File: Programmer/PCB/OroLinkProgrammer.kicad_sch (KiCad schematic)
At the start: 17 parts, among them IC1 SE555DR, J1 67996-110HLF, M1 STM32 STLINK V3MODS

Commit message: re-layout board onto new PCB
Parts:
- removed H1, H2, H3: MountingHole, MountingHole:MountingHole_3.2mm_M3_Pad_Via, symbol Mechanical:MountingHole
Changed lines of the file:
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@@
   )
   (text "NOTE: BOM COMPONENTS DO NOT INCLUDE\n        2x5 2.54mm-PITCH CABLE TERMINAL,\n        BUT ONE IS REQUIRED (CHECK\n        PCB FOR PINOUT, AND TAKE\n        NOTE OF NOTCH SPECIFICATION)"
-    (at 191.77 147.32 0)
+    (at 177.165 147.955 0)
     (effects (font (size 1.27 1.27)) (justify left bottom))
   )
@@
         (path "/fd4a9034-ad51-4795-b47c-26ad06998c0c"
           (reference "#PWR02") (unit 1)
-        )
-      )
-    )
-  )
-  (symbol (lib_id "Mechanical:MountingHole") (at 165.735 135.255 0) (unit 1)
-    (in_bom no) (on_board yes) (dnp no)
-    (property "Reference" "H2" (at 168.91 135.255 0)
-      (effects (font (size 1.27 1.27)) (justify left))
-    )
-    (property "Value" "MountingHole" (at 168.275 136.5323 0)
-      (effects (font (size 1.27 1.27)) (justify left) hide)
-    )
-    (property "Footprint" "MountingHole:MountingHole_3.2mm_M3_Pad_Via" (at 165.735 135.255 0)
-      (effects (font (size 1.27 1.27)) hide)
-    )
-    (property "Datasheet" "~" (at 165.735 135.255 0)
-      (effects (font (size 1.27 1.27)) hide)
-    )
-    (property "Sim.Enable" "0" (at 165.735 135.255 0)
-      (effects (font (size 1.27 1.27)) hide)
-    )
-    (instances
-      (project "OroLinkProgrammer"
-        (path "/fd4a9034-ad51-4795-b47c-26ad06998c0c"
-          (reference "H2") (unit 1)
-        )
-      )
-    )
-  )
-  (symbol (lib_id "Mechanical:MountingHole") (at 165.735 130.175 0) (unit 1)
-    (in_bom no) (on_board yes) (dnp no)
-    (property "Reference" "H1" (at 168.91 130.175 0)
-      (effects (font (size 1.27 1.27)) (justify left))
-    )
-    (property "Value" "MountingHole" (at 168.275 131.4523 0)
-      (effects (font (size 1.27 1.27)) (justify left) hide)
-    )
-    (property "Footprint" "MountingHole:MountingHole_3.2mm_M3_Pad_Via" (at 165.735 130.175 0)
-      (effects (font (size 1.27 1.27)) hide)
-    )
-    (property "Datasheet" "~" (at 165.735 130.175 0)
-      (effects (font (size 1.27 1.27)) hide)
-    )
-    (property "Sim.Enable" "0" (at 165.735 130.175 0)
-      (effects (font (size 1.27 1.27)) hide)
-    )
-    (instances
-      (project "OroLinkProgrammer"
-        (path "/fd4a9034-ad51-4795-b47c-26ad06998c0c"
-          (reference "H1") (unit 1)
         )
       )
@@
     )
   )
-  (symbol (lib_id "Mechanical:MountingHole") (at 165.735 140.335 0) (unit 1)
-    (in_bom no) (on_board yes) (dnp no)
-    (property "Reference" "H3" (at 168.91 140.335 0)
-      (effects (font (size 1.27 1.27)) (justify left))
-    )
-    (property "Value" "MountingHole" (at 168.275 141.6123 0)
-      (effects (font (size 1.27 1.27)) (justify left) hide)
-    )
-    (property "Footprint" "MountingHole:MountingHole_3.2mm_M3_Pad_Via" (at 165.735 140.335 0)
-      (effects (font (size 1.27 1.27)) hide)
-    )
-    (property "Datasheet" "~" (at 165.735 140.335 0)
-      (effects (font (size 1.27 1.27)) hide)
-    )
-    (property "Sim.Enable" "0" (at 165.735 140.335 0)
-      (effects (font (size 1.27 1.27)) hide)
-    )
-    (instances
-      (project "OroLinkProgrammer"
-        (path "/fd4a9034-ad51-4795-b47c-26ad06998c0c"
-          (reference "H3") (unit 1)
-        )
-      )
-    )
-  )
   (symbol (lib_id "SamacSys_Parts:SG73P2ATTD102J") (at 83.82 42.545 180) (unit 1)
     (in_bom yes) (on_board yes) (dnp no) (fields_autoplaced)
@@
     )
   )
-  (symbol (lib_id "Oro:BOM Part") (at 193.675 132.715 0) (unit 1)
+  (symbol (lib_id "Oro:BOM Part") (at 179.07 133.35 0) (unit 1)
     (in_bom yes) (on_board no) (dnp no)
-    (property "Reference" "B2" (at 195.58 132.0713 0)
-      (effects (font (size 1.27 1.27)) (justify left) hide)
-    )
-    (property "Value" "S-3-J-7-G" (at 196.215 133.985 0)
+    (property "Reference" "B2" (at 180.975 132.7063 0)
+      (effects (font (size 1.27 1.27)) (justify left) hide)
+    )
+    (property "Value" "S-3-J-7-G" (at 181.61 134.62 0)
       (effects (font (size 1.27 1.27)) (justify left))
     )
-    (property "Footprint" "" (at 193.675 132.715 0)
-      (effects (font (size 1.27 1.27)) hide)
-    )
-    (property "Datasheet" "https://www.mouser.de/datasheet/2/193/F_SINT_Board_Test_StandardSpringProbes_0125Centers-2308876.pdf" (at 193.675 132.715 0)
-      (effects (font (size 1.27 1.27)) hide)
-    )
-    (property "Sim.Enable" "0" (at 193.675 132.715 0)
-      (effects (font (size 1.27 1.27)) hide)
-    )
-    (property "Manufacturer_Part_Number" "R-3-CR" (at 193.675 132.715 0)
-      (effects (font (size 1.27 1.27)) hide)
-    )
-    (property "Mouser Part Number" "S-3-J-7-G" (at 193.675 132.715 0)
-      (effects (font (size 1.27 1.27)) hide)
-    )
-    (property "Note" "TEST PROBE" (at 196.215 132.715 0)
+    (property "Footprint" "" (at 179.07 133.35 0)
+      (effects (font (size 1.27 1.27)) hide)
+    )
+    (property "Datasheet" "https://www.mouser.de/datasheet/2/193/F_SINT_Board_Test_StandardSpringProbes_0125Centers-2308876.pdf" (at 179.07 133.35 0)
+      (effects (font (size 1.27 1.27)) hide)
+    )
+    (property "Sim.Enable" "0" (at 179.07 133.35 0)
+      (effects (font (size 1.27 1.27)) hide)
+    )
+    (property "Manufacturer_Part_Number" "R-3-CR" (at 179.07 133.35 0)
+      (effects (font (size 1.27 1.27)) hide)
+    )
+    (property "Mouser Part Number" "S-3-J-7-G" (at 179.07 133.35 0)
+      (effects (font (size 1.27 1.27)) hide)
+    )
+    (property "Note" "TEST PROBE" (at 181.61 133.35 0)
       (effects (font (size 1.27 1.27)) (justify left bottom))
     )
-    (property "BOM Qty" "6" (at 193.675 132.715 0)
+    (property "BOM Qty" "6" (at 179.07 133.35 0)
       (effects (font (size 1.27 1.27)) hide)
     )
@@
     )
   )
-  (symbol (lib_id "Oro:BOM Part") (at 193.675 125.73 0) (unit 1)
+  (symbol (lib_id "Oro:BOM Part") (at 179.07 126.365 0) (unit 1)
     (in_bom yes) (on_board no) (dnp no)
-    (property "Reference" "B2" (at 195.58 125.0863 0)
-      (effects (font (size 1.27 1.27)) (justify left) hide)
-    )
-    (property "Value" "R-3-CR" (at 196.215 127 0)
+    (property "Reference" "B2" (at 180.975 125.7213 0)
+      (effects (font (size 1.27 1.27)) (justify left) hide)
+    )
+    (property "Value" "R-3-CR" (at 181.61 127.635 0)
       (effects (font (size 1.27 1.27)) (justify left))
     )
-    (property "Footprint" "" (at 193.675 125.73 0)
-      (effects (font (size 1.27 1.27)) hide)
-    )
-    (property "Datasheet" "https://www.mouser.de/datasheet/2/193/ICDIS00002_1-2550070.pdf" (at 193.675 125.73 0)
-      (effects (font (size 1.27 1.27)) hide)
-    )
-    (property "Sim.Enable" "0" (at 193.675 125.73 0)
-      (effects (font (size 1.27 1.27)) hide)
-    )
-    (property "Manufacturer_Part_Number" "R-3-CR" (at 193.675 125.73 0)
-      (effects (font (size 1.27 1.27)) hide)
-    )
-    (property "Mouser Part Number" "818-R-3-CR" (at 193.675 125.73 0)
-      (effects (font (size 1.27 1.27)) hide)
-    )
-    (property "Note" "TEST PROBE CRIMP SOCKET" (at 196.215 125.73 0)
+    (property "Footprint" "" (at 179.07 126.365 0)
+      (effects (font (size 1.27 1.27)) hide)
+    )
+    (property "Datasheet" "https://www.mouser.de/datasheet/2/193/ICDIS00002_1-2550070.pdf" (at 179.07 126.365 0)
+      (effects (font (size 1.27 1.27)) hide)
+    )
+    (property "Sim.Enable" "0" (at 179.07 126.365 0)
+      (effects (font (size 1.27 1.27)) hide)
+    )
+    (property "Manufacturer_Part_Number" "R-3-CR" (at 179.07 126.365 0)
+      (effects (font (size 1.27 1.27)) hide)
+    )
+    (property "Mouser Part Number" "818-R-3-CR" (at 179.07 126.365 0)
+      (effects (font (size 1.27 1.27)) hide)
+    )
+    (property "Note" "TEST PROBE CRIMP SOCKET" (at 181.61 126.365 0)
       (effects (font (size 1.27 1.27)) (justify left bottom))
     )
-    (property "BOM Qty" "6" (at 193.675 125.73 0)
-      (effects (font (size 1.27 1.27)) hide)
-    )
+    (property "BOM Qty" "6" (at 179.07 126.365 0)
+      (effects (font (size 1.27 1.27)) hide)
+    )

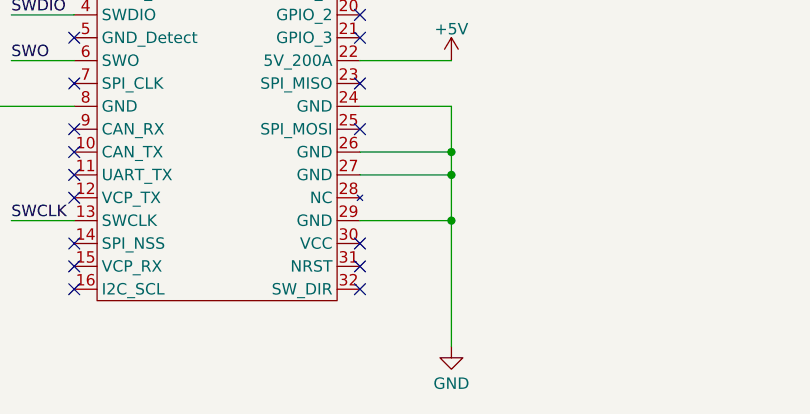
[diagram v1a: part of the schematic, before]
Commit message: tie NRST to ground on programmer (closes #4)
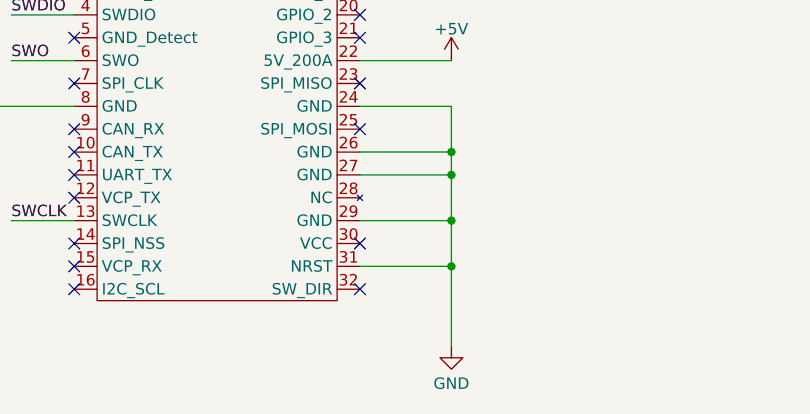
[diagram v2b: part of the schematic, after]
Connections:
- net GND: now also M1.31 (NRST)
- no-connect marks 33 -> 32
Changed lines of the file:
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@@
   (junction (at 229.235 93.345) (diameter 0) (color 0 0 0 0)
+  )
+  (junction (at 135.255 153.67) (diameter 0) (color 0 0 0 0)
   )
   (junction (at 186.69 55.88) (diameter 0) (color 0 0 0 0)
@@
   (no_connect (at 93.345 140.97))
   (no_connect (at 93.345 151.13))
-  (no_connect (at 125.095 153.67))
   (no_connect (at 93.345 156.21))
   (no_connect (at 125.095 118.11))
@@
   (no_connect (at 93.98 66.04))
   (no_connect (at 125.095 156.21))
+  (wire (pts (xy 125.095 153.67) (xy 135.255 153.67))
+    (stroke (width 0) (type default))
+  )
   (wire (pts (xy 43.815 42.545) (xy 47.625 42.545))
     (stroke (width 0) (type default))
@@
   )
   (wire (pts (xy 124.46 60.96) (xy 132.08 60.96))
+    (stroke (width 0) (type default))
+  )
+  (wire (pts (xy 135.255 153.67) (xy 135.255 162.56))
     (stroke (width 0) (type default))
   )
@@
     (stroke (width 0) (type default))
   )
-  (wire (pts (xy 135.255 148.59) (xy 135.255 162.56))
+  (wire (pts (xy 135.255 148.59) (xy 135.255 153.67))
     (stroke (width 0) (type default))
   )

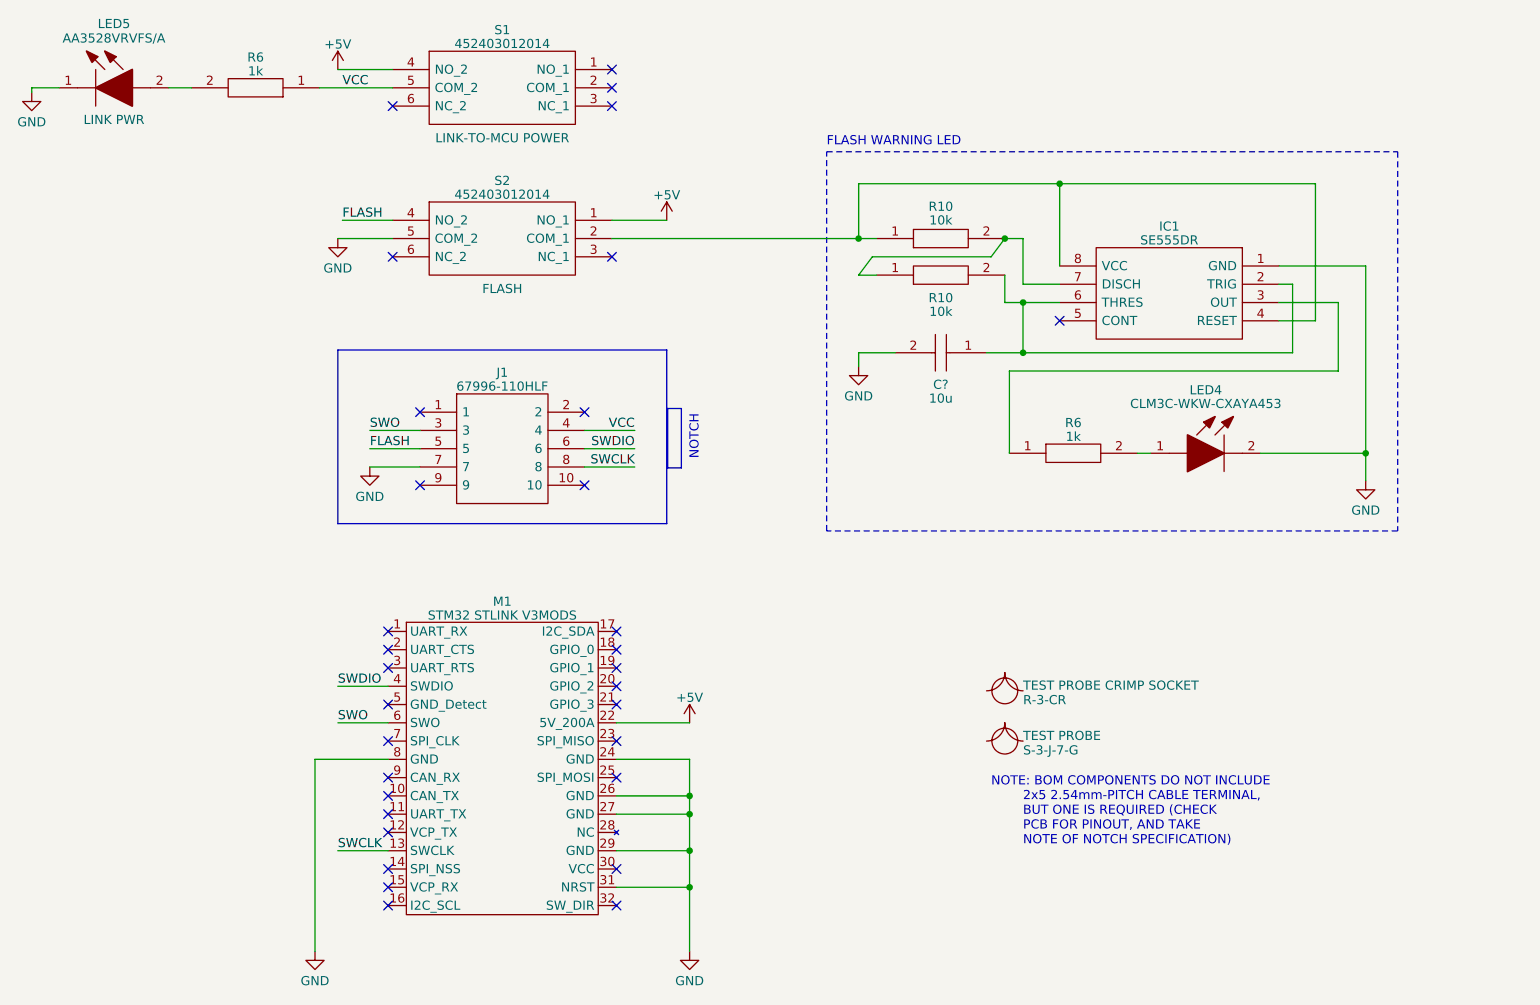
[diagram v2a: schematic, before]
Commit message: change boot configuration lines and switches; replace 555 with 3v3 vers.
ref #3
closes #5
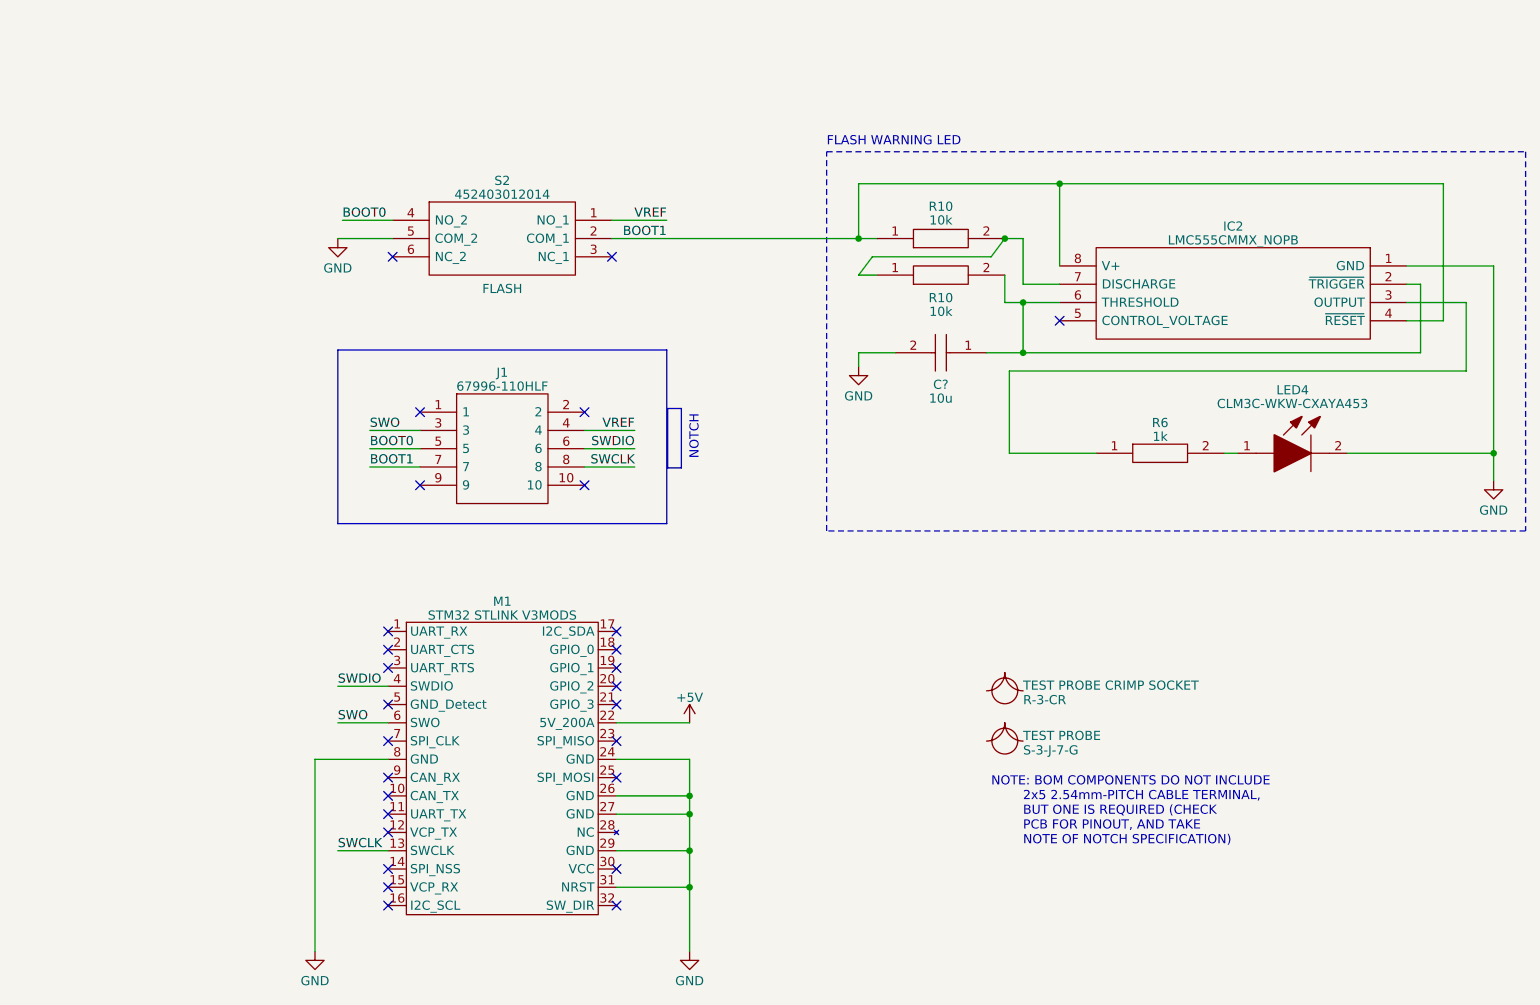
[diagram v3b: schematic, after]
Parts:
- removed IC1: SE555DR, SOIC127P600X175-8N, symbol SamacSys_Parts:SE555DR
- removed LED5: AA3528VRVFS/A, SamacSys_Parts:AA3528VRVFSA, symbol SamacSys_Parts:AA3528VRVFS_A
- removed R6: 1k, RESC2012X60N, symbol SamacSys_Parts:SG73P2ATTD102J
- removed S1: 452403012014, 452403012014, symbol SamacSys_Parts:452403012014
- added IC2: LMC555CMMX_NOPB, SOP65P490X110-8N, symbol SamacSys_Parts:LMC555CMMX_NOPB
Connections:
- net +5V: no longer S2.1 (NO_1)
- net GND: now also IC2.1 (GND); no longer J1.7
- net at C?.1, R10.2: now also IC2.2 (~{TRIGGER}), IC2.6 (THRESHOLD)
- net at R6.1: now also IC2.3 (OUTPUT)
- net BOOT1: now reaches R10.1, S2.2 (COM_1)
- net BOOT1: now also J1.7, IC2.4 (~{RESET}), IC2.8 (V+)
- net at R10.1, R10.2: now also IC2.7 (DISCHARGE)
- net FLASH renamed BOOT0
- net VCC renamed VREF
- net VREF: now also S2.1 (NO_1)
- no-connect marks 32 -> 28
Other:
- moved on the sheet: LED4, R6

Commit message: add debug tht's to programmer (closes #8)
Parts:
- added DBG35 (x5): ~, Oro Footprints:DebugPin, symbol Oro:DebugPin
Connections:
- net GND: now also DBG35.1
- net SWCLK: now also DBG35.1
- net SWDIO: now also DBG35.1
- net SWO: now also DBG35.1
- net VREF: now also M1.30 (VCC), DBG35.1
- net +5V: no longer names the net of M1.22 (5V_200A)
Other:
- note added: "DEBUG THTS"

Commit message: fix mouser and mfr ID for programmer test probes
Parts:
- B2: Manufacturer_Part_Number R-3-CR -> S-3-J-7-G; Mouser Part Number S-3-J-7-G -> 818-S-3-J-7-G
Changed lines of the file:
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@@
       (effects (font (size 1.27 1.27)) hide)
     )
-    (property "Manufacturer_Part_Number" "R-3-CR" (at 179.07 133.35 0)
+    (property "Manufacturer_Part_Number" "S-3-J-7-G" (at 179.07 133.35 0)
       (effects (font (size 1.27 1.27)) hide)
     )
-    (property "Mouser Part Number" "S-3-J-7-G" (at 179.07 133.35 0)
+    (property "Mouser Part Number" "818-S-3-J-7-G" (at 179.07 133.35 0)
       (effects (font (size 1.27 1.27)) hide)
     )
